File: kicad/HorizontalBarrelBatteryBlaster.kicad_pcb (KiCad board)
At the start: 2 copper layers, 22.2 x 13.5 mm, 5 parts

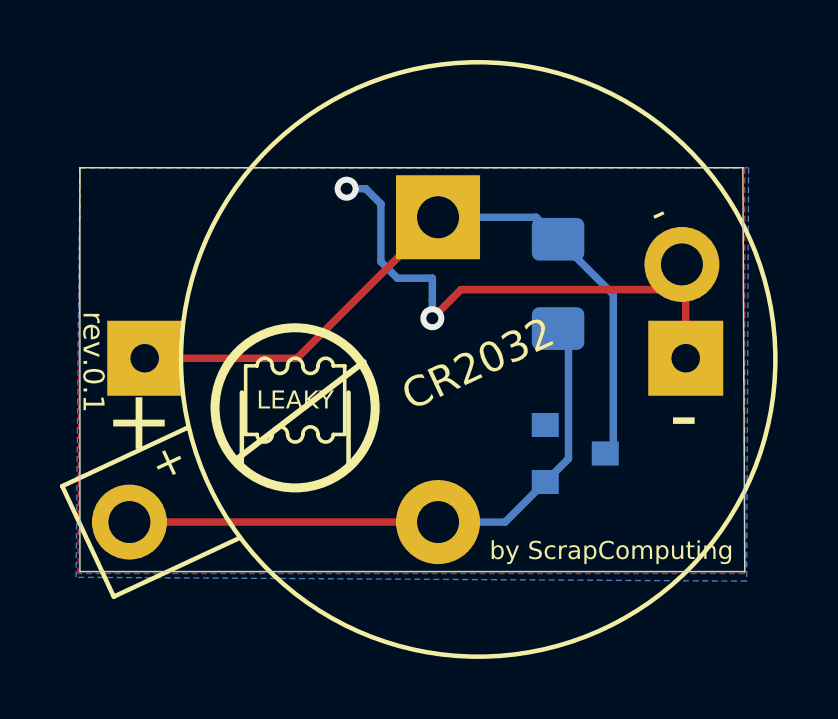
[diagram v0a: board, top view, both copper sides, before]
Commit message: Includes solder pads for MAX40200 ideal diode
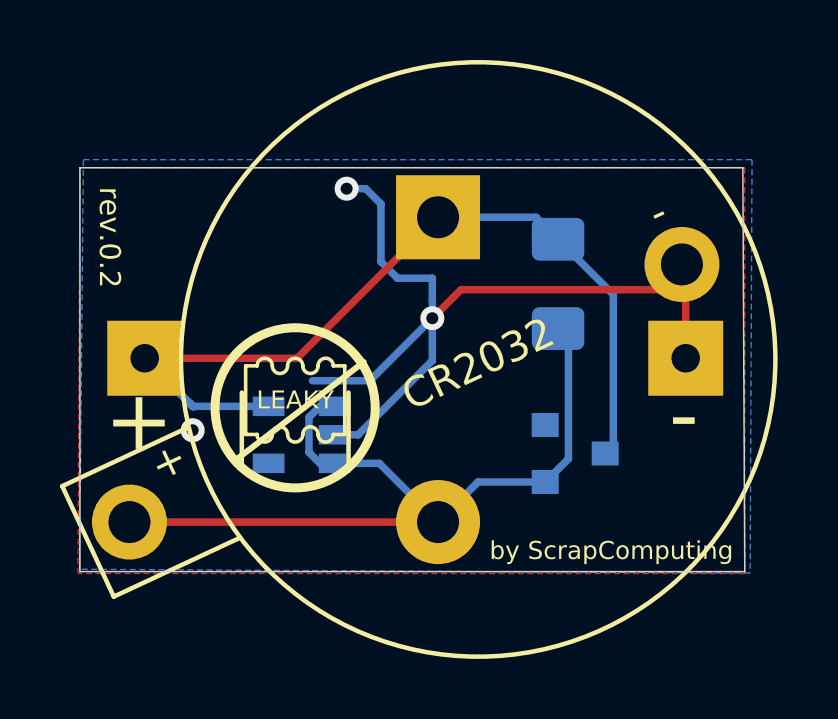
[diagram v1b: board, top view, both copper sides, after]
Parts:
- added U1: MAX40200AUK, Package_TO_SOT_SMD:SOT-23-5, B.Cu at (219.4, 72.3)
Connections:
- net /GND renamed GND
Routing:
- net GND: track 18.8 -> 29.3 mm, vias 2 -> 3
- net Net-(BarrelBattery1-Pad1): track 24.0 -> 32.5 mm
- net /3V: track 20.0 -> 27.4 mm
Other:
- board text added: "MAX40200"
- board text added: "ScrapComputing"
- board text added: "rev.0.2"
- board text removed: "rev.0.1"
